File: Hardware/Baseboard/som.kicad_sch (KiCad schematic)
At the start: 0 parts

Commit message: BB SOM connector
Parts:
- added J2: 1473005-4, FPGA4RISCV:14730054, symbol FPGA4RISCV:1473005-4
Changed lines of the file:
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@@
 	(generator "eeschema")
 	(generator_version "9.0")
-	(paper "A4")
-)
+	(paper "A3" portrait)

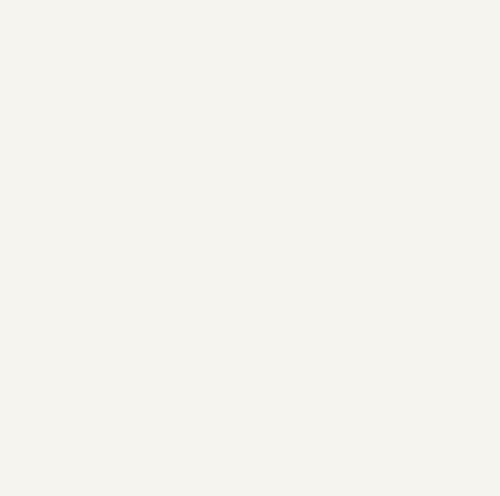
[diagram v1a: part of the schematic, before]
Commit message: QSPI, banks IO decoupling
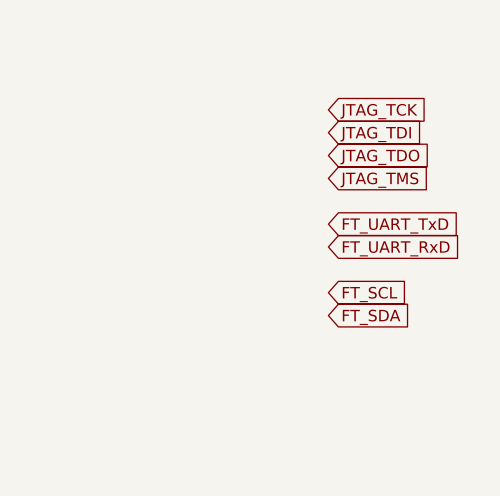
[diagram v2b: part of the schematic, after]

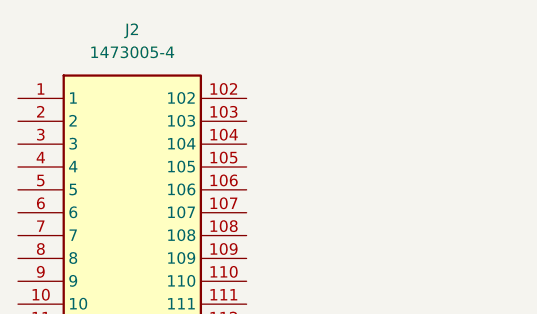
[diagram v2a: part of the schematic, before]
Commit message: PCIe M.2 connector changed
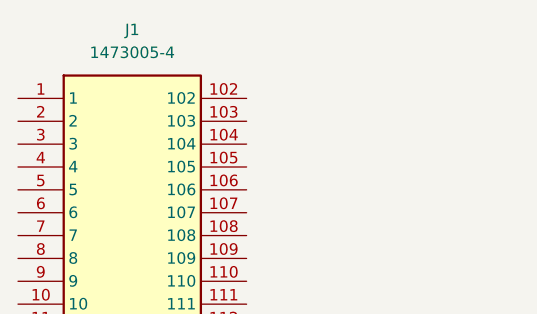
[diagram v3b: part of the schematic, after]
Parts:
- renumbered J2 to J1

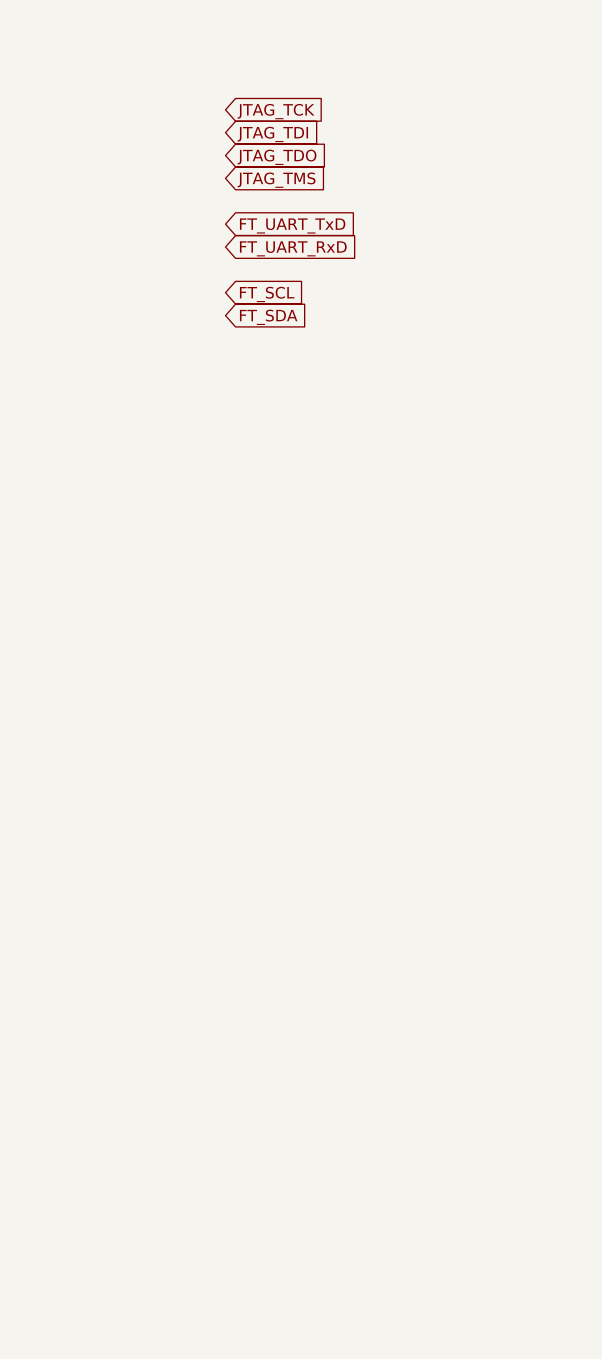
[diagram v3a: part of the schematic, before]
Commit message: PCIe M.2 pull-ups
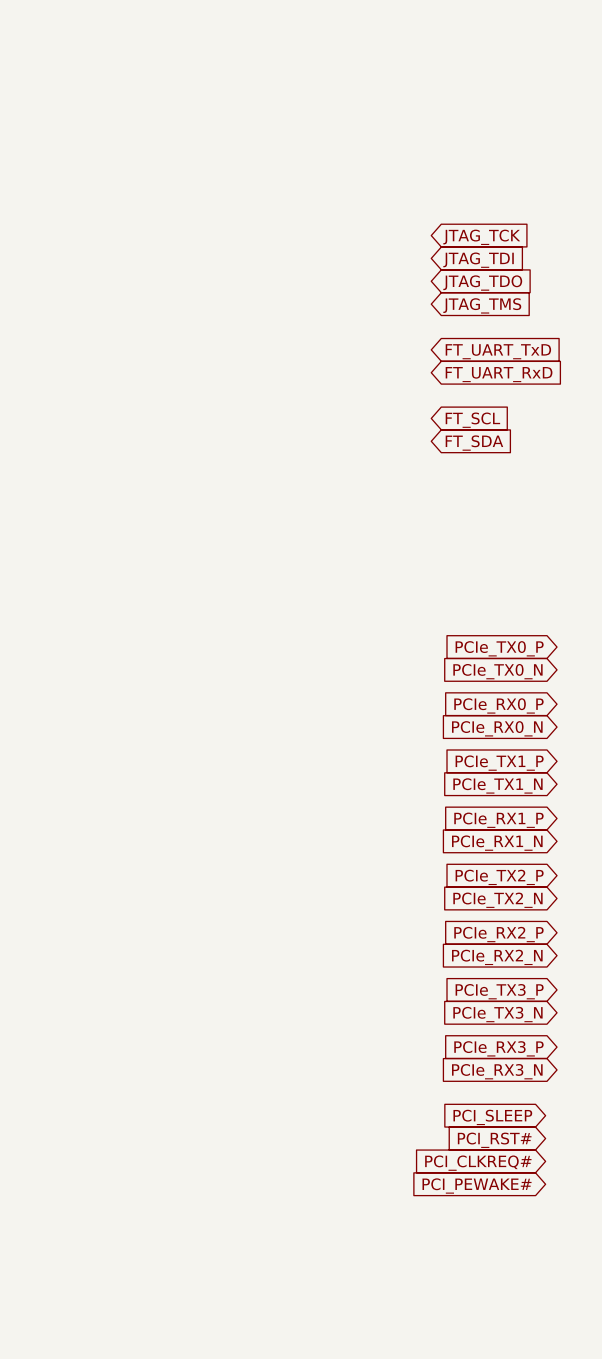
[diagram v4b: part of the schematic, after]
